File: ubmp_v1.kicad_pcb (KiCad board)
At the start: 2 copper layers, 34.5 x 14 mm, 34 parts, among them J1 Conn_02x05_Counter_Clockwise, J2 USB_A, U1 STM32F103CBUx, U2 MIC5245-3.3, Y1 PRQC8.00CR1010V00L

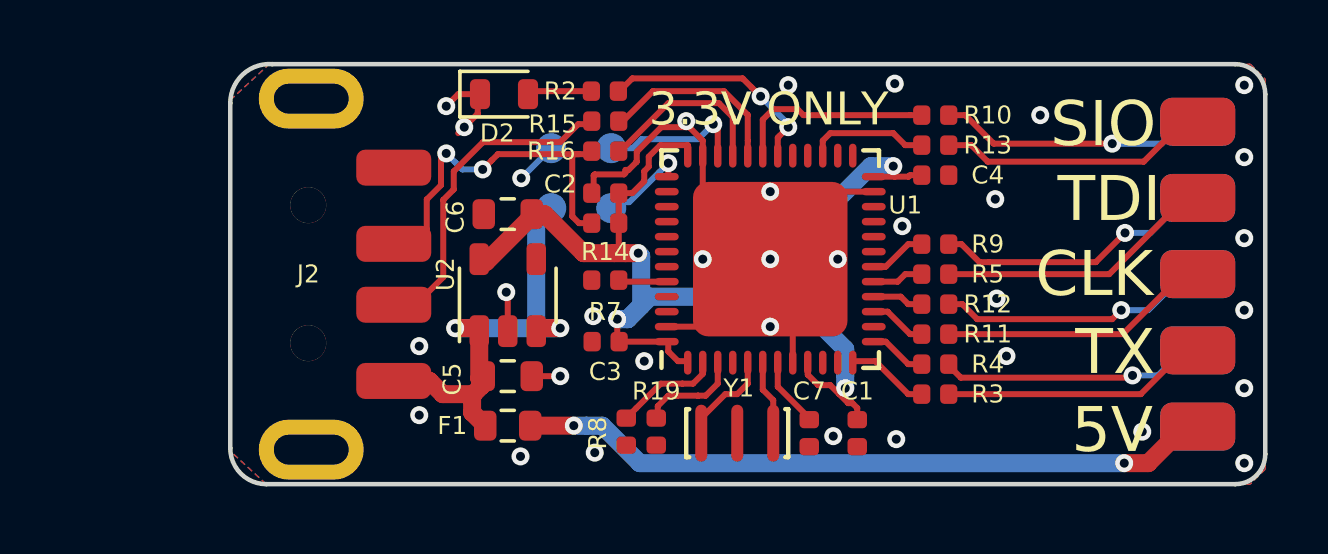
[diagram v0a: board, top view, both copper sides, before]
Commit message: Split into hierarchical sheep
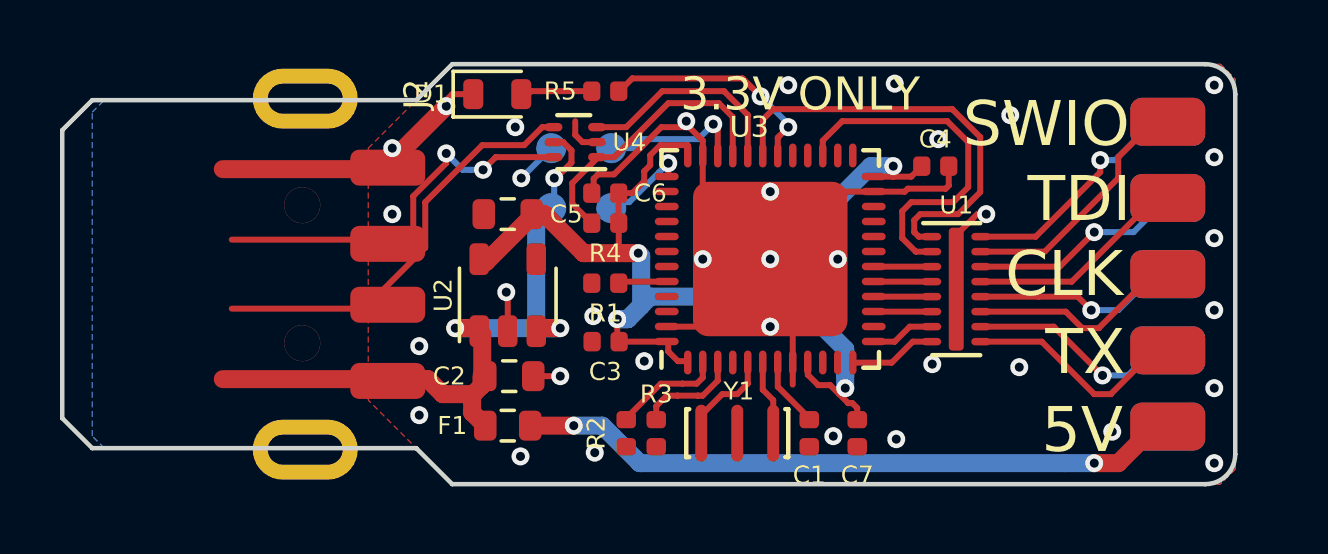
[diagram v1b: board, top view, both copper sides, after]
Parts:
- removed D2: GREEN, ubmp:D_0603_1608Metric_Rounded
- removed R10, R11, R12, R13: 100, ubmp:R_0402_1005Metric_Rounded
- removed R14, R19, R7, R8: 1.5k, ubmp:R_0402_1005Metric_Rounded
- removed R15, R16, R9: 22, ubmp:R_0402_1005Metric_Rounded
- added D1: GREEN, ubmp:D_0603_1608Metric_Rounded, F.Cu at (93.9, 100.0)
- added R1: 1.5k, ubmp:R_0402_1005Metric_Rounded, F.Cu at (97.5, 106.3)
- added U3: STM32F103CBUx, ubmp:QFN-48-1EP_7x7mm_P0.5mm_EP5.15x5.15mm, F.Cu at (103.0, 105.5)
- added U4: NUF2042XV6T1G, ubmp:DFN-6-1EP_1.2x1.6mm_P0.5mm, F.Cu at (96.5, 101.6)
- C2: value 100n -> 4.7u; footprint ubmp:C_0402_1005Metric_Rounded -> ubmp:C_0603_1608Metric_Rounded
- C6: value 4.7u -> 100n; footprint ubmp:C_0603_1608Metric_Rounded -> ubmp:C_0402_1005Metric_Rounded
- R2: value 470 -> 1.5k
- R3, R4: value 100 -> 1.5k
- R5: value 100 -> 470
- U1: value STM32F103CBUx -> NUF8401MNT4G; footprint ubmp:QFN-48-1EP_7x7mm_P0.5mm_EP5.15x5.15mm -> ubmp:DFN-16-1EP_1.6x4mm_P0.5mm
- moved R5 12.6 mm to (97.5, 99.9)
- moved R4 12.0 mm to (97.5, 104.3)
- moved R2 11.4 mm to (98.2, 111.3), turned to 270 degrees
- moved R3 9.39 mm to (99.2, 111.3), turned to 270 degrees
- moved C2 6.89 mm to (94.3, 109.4), turned to 0 degrees
- moved U1 6.28 mm to (109.2, 106.5), turned to 0 degrees
- moved C5 5.40 mm to (94.2, 104.0), turned to 180 degrees
- moved C6 3.32 mm to (97.5, 103.3)
- moved C1 1.60 mm to (104.3, 111.3), turned to 90 degrees
- moved C7 1.60 mm to (105.9, 111.3), turned to 270 degrees
- moved J1 1.00 mm to (116.2, 106.0)
- moved C4 0.30 mm to (108.5, 102.4)
- moved J2 0.20 mm to (89.5, 106.0)
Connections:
- C1 pad 1: +3V3 -> GND
- C1 pad 2: GND -> /bmp_core/NRST
- C2 pad 1: +3V3 -> +5V
- C5 pad 1: +5V -> +3V3
- C7 pad 1: GND -> +3V3
- C7 pad 2: /NRST -> GND
- J1 pad 2: /BMP_TXo -> /bmp_core/BMP_TXo
- J1 pad 3: /BMP_SWCLK_TCKo -> /bmp_core/BMP_SWCLK_TCKo
- J1 pad 4: /BMP_TDIo -> /bmp_core/BMP_TDIo
- J1 pad 5: /BMP_SWDIO_TMSo -> /bmp_core/BMP_SWDIO_TMSo
- J1 pad 6: /BMP_SWOo -> /bmp_core/BMP_SWOo
- J1 pad 7: /BMP_RSTo -> /bmp_core/BMP_RSTo
- J1 pad 8: /BMP_TDOo -> /bmp_core/BMP_TDOo
- J1 pad 9: /BMP_RXo -> /bmp_core/BMP_RXo
- R2 pad 1: /LED_STLINK -> /bmp_core/STM_ID
- R2 pad 2: Net-(D2-Pad2) -> GND
- R3 pad 1: /BMP_TXo -> /bmp_core/STM_ID2
- R3 pad 2: /BMP_TX -> GND
- R4 pad 1: /BMP_RXo -> +3V3
- R4 pad 2: /BMP_RX -> /bmp_core/DP_P
- R5 pad 1: /BMP_TDIo -> /bmp_core/LED_STLINK
- R5 pad 2: /BMP_TDI -> Net-(D1-Pad2)
- TP1 pad 1: /SWDIO -> /bmp_core/SWDIO
- TP2 pad 1: /SWCLK -> /bmp_core/SWCLK
- U1 pad 1: +3V3 -> /bmp_core/BMP_SWO
- U1 pad 10: Net-(U1-Pad10) -> /bmp_core/BMP_RXo
- U1 pad 11: Net-(U1-Pad11) -> /bmp_core/BMP_SWCLK_TCKo
- U1 pad 12: /BMP_TX -> /bmp_core/BMP_TDOo
- U1 pad 13: /BMP_RX -> /bmp_core/BMP_TDIo
- U1 pad 14: Net-(U1-Pad14) -> /bmp_core/BMP_RSTo
- U1 pad 15: /BMP_SWCLK_TCK -> /bmp_core/BMP_SWDIO_TMSo
- U1 pad 16: /BMP_TDO -> /bmp_core/BMP_SWOo
- U1 pad 17: /BMP_TDI -> GND
- U1 pad 2: /STM_ID -> /bmp_core/BMP_SWDIO_TMS
- U1 pad 3: /STM_ID2 -> /bmp_core/BMP_RST
- U1 pad 4: Net-(U1-Pad4) -> /bmp_core/BMP_TDI
- U1 pad 5: Net-(U1-Pad5) -> /bmp_core/BMP_TDO
- U1 pad 6: Net-(U1-Pad6) -> /bmp_core/BMP_SWCLK_TCK
- U1 pad 7: /NRST -> /bmp_core/BMP_RX
- U1 pad 8: GND -> /bmp_core/BMP_TX
- U1 pad 9: +3V3 -> /bmp_core/BMP_TXo
- Y1 pad 1: Net-(U1-Pad5) -> Net-(U3-Pad5)
- Y1 pad 3: Net-(U1-Pad6) -> Net-(U3-Pad6)
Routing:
- net GND: track 29.6 -> 44.1 mm, vias 33 -> 35
- net /bmp_core/BMP_SWO: track 0.00 -> 14.5 mm
- net /bmp_core/BMP_SWDIO_TMS: track 0.00 -> 12.1 mm
- net /bmp_core/DP_P: track 0.00 -> 9.57 mm
- net /BMP_RSTo: track 9.50 -> 0.00 mm, vias 1 -> 0
- net /BMP_TDIo: track 9.41 -> 0.00 mm
- net /BMP_SWCLK_TCKo: track 9.19 -> 0.00 mm
- net /BMP_TDOo: track 9.19 -> 0.00 mm, vias 1 -> 0
- net /BMP_SWDIO_TMSo: track 9.08 -> 0.00 mm
- net /BMP_SWOo: track 9.00 -> 0.00 mm, vias 1 -> 0
- net /BMP_TXo: track 8.97 -> 0.00 mm
- net /BMP_RXo: track 8.93 -> 0.00 mm, vias 1 -> 0
- net /bmp_core/BMP_SWDIO_TMSo: track 0.00 -> 8.43 mm
- net /bmp_core/BMP_SWOo: track 0.00 -> 8.05 mm, vias 0 -> 1
- net /bmp_core/LED_STLINK: track 0.00 -> 7.82 mm, vias 0 -> 2
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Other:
- board size 34.5 x 14 mm -> 39.1 x 14 mm
- board text added: "SWIO"
- board text added: "µBMP v1.2"
- board text removed: "SIO"
- board text removed: "µBMP v1.1"

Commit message: Updated pinput
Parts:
- moved R4 0.10 mm to (97.5, 104.4)
- moved J2 0.10 mm to (89.6, 106.0)
- moved R3 0.10 mm to (99.3, 111.3)
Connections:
- J1 pad 4: /bmp_core/BMP_TDIo -> /bmp_core/BMP_RSTo
- J1 pad 7: /bmp_core/BMP_RSTo -> /bmp_core/BMP_TDIo
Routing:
- net GND: track 44.1 -> 35.8 mm
- net +5V: track 24.6 -> 17.8 mm
- net /DP: track 13.3 -> 8.19 mm
- net /DM: track 14.1 -> 9.68 mm
- net /bmp_core/BMP_RSTo: vias 1 -> 0
- net /bmp_core/BMP_TDIo: vias 0 -> 1
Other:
- board size 39.1 x 14 mm -> 33.5 x 14 mm

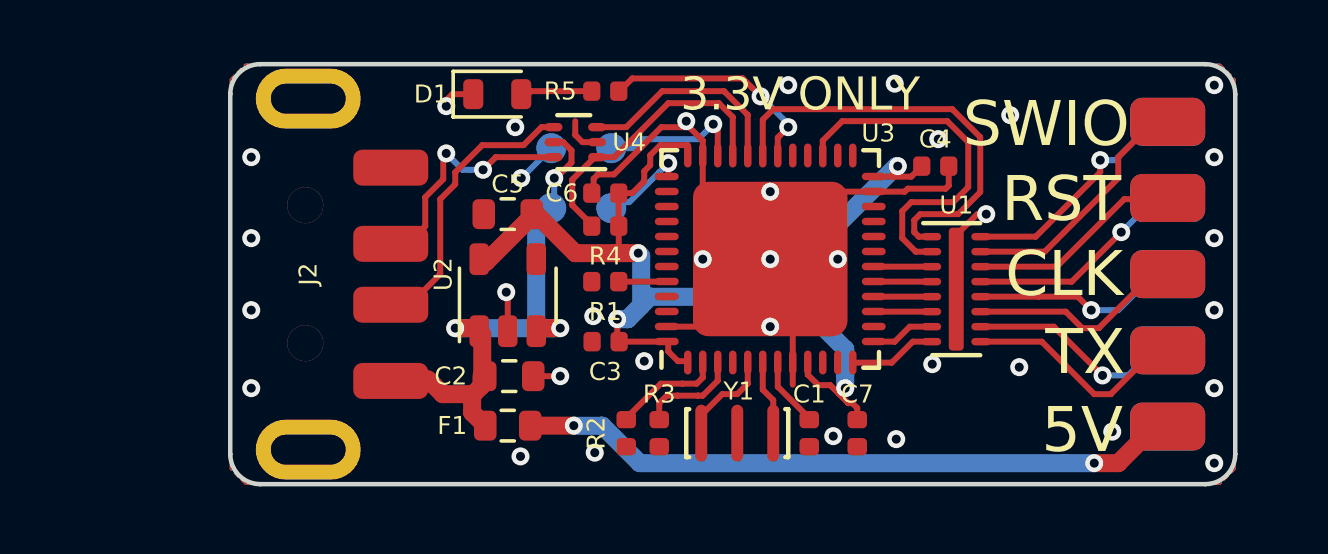
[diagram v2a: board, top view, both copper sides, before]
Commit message: Moved libs to external repo
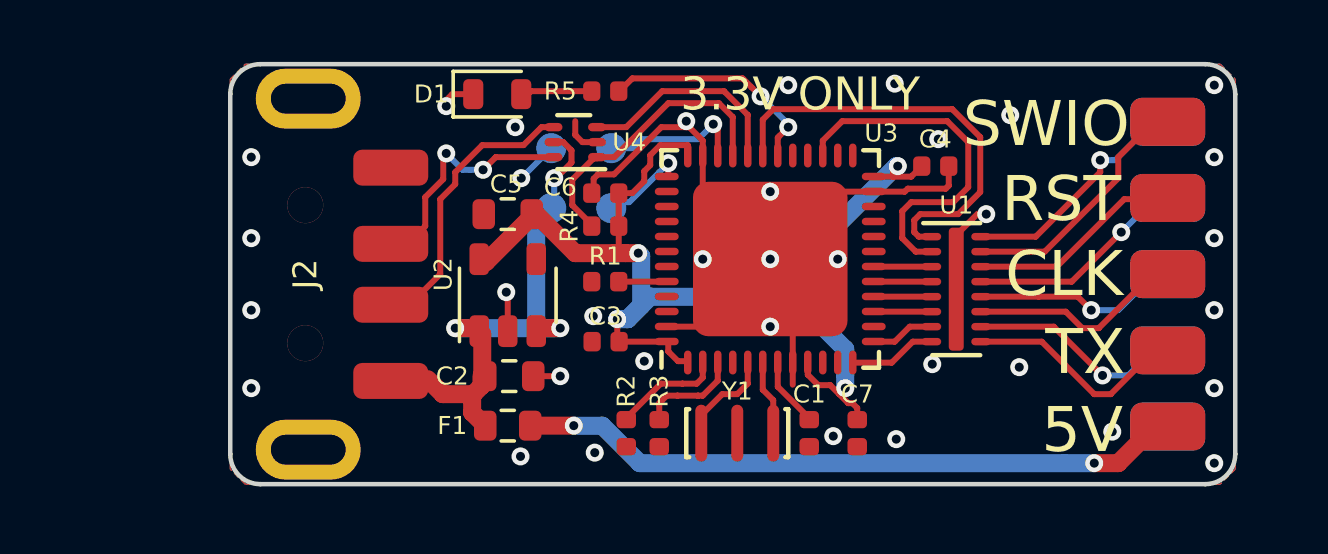
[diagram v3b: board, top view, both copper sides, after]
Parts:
- C1, C3, C4, C6, C7: footprint ubmp:C_0402_1005Metric_Rounded -> passive:C_0402_1005Metric_Rounded
- C2, C5: footprint ubmp:C_0603_1608Metric_Rounded -> passive:C_0603_1608Metric_Rounded
- D1: footprint ubmp:D_0603_1608Metric_Rounded -> passive:D_0603_1608Metric_Rounded
- F1: footprint ubmp:R_0603_1608Metric_Rounded -> passive:R_0603_1608Metric_Rounded
- J1: footprint ubmp:2x5_2.54mm_side -> connectors:2x5_2.54mm_side
- J2: footprint usbpcb:USB_A_1001-011-01101 -> usb:USB_A_1001-011-01101
- R1, R2, R3, R4, R5: footprint ubmp:R_0402_1005Metric_Rounded -> passive:R_0402_1005Metric_Rounded
- U1: footprint ubmp:DFN-16-1EP_1.6x4mm_P0.5mm -> dfn:DFN-16-1EP_1.6x4mm_P0.5mm
- U2: footprint ubmp:SOT-23-5_Rounded -> sot:SOT-23-5
- U3: footprint ubmp:QFN-48-1EP_7x7mm_P0.5mm_EP5.15x5.15mm -> qfn:QFN-48-1EP_7x7mm_P0.5mm_EP5.15x5.15mm
- U4: footprint ubmp:DFN-6-1EP_1.2x1.6mm_P0.5mm -> dfn:DFN-6-1EP_1.2x1.6mm_P0.5mm
- Y1: footprint ubmp:Resonator_3pin_3.2x1.3mm -> crystals:Resonator_3pin_3.2x1.3mm
